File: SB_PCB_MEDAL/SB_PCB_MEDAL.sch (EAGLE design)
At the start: 10 parts, among them IC1 ATTINY44A-SSU

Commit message: completed circuit for charliplexed LEDs
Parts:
- added LED10, LED11, LED12, LED13, LED14, LED15, LED16, LED18, LED19, LED2, LED20, LED21, LED22, LED23, LED24, LED25, LED26, LED27, LED28, LED29, LED3, LED30, LED31, LED32, LED33, LED4, LED5, LED6, LED7, LED8, LED9: KPT-2012CGCK, SamacSys_Parts:KPT-2012CGCK
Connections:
- new net N$1: LED26.A
- new net N$10: LED2.A, LED4.K
- new net N$2: LED3.K, LED5.A, LED7.A
- new net N$3: LED1.K, LED3.A
- new net N$4: LED5.K, LED7.K, LED8.A, LED9.A
- new net N$5: LED11.A, LED8.K, LED9.K
- new net N$6: LED10.A, LED12.K
- new net N$7: LED10.K, LED6.A
- new net N$8: LED4.A, LED6.K
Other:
- moved on the sheet: R2, R3, R4, R5, R6

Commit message: re-did some wiring
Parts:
- removed LED31, LED32, LED33: KPT-2012CGCK, SamacSys_Parts:KPT-2012CGCK
- added LED17: KPT-2012CGCK, SamacSys_Parts:KPT-2012CGCK
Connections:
- removed net N$10: LED2.A, LED4.K
- removed net N$7: LED10.K, LED6.A
- removed net N$8: LED4.A, LED6.K
- net N$1: now also LED1.A, LED11.A, LED12.K, LED19.A, LED2.K, LED20.K, LED25.A, LED26.K, LED29.A, LED30.K, R1.2; no longer LED26.A
- net N$2: now also LED1.K, LED13.A, LED14.K, LED2.A, LED21.A, LED22.K, LED27.A, LED28.K, LED3.A, LED4.K, R2.2; no longer LED3.K, LED5.A, LED7.A
- net N$3: now also LED11.K, LED12.A, LED15.A, LED16.K, LED23.A, LED24.K, LED3.K, LED4.A, LED5.A, LED6.K, R3.2; no longer LED1.K, LED3.A
- net N$4: now also LED13.K, LED14.A, LED17.A, LED18.K, LED19.K, LED20.A, LED6.A, LED7.A, LED8.K, R4.2; no longer LED7.K, LED8.A, LED9.A
- net N$5: now also LED10.K, LED15.K, LED16.A, LED21.K, LED22.A, LED25.K, LED26.A, LED7.K, LED8.A, LED9.A, R5.2; no longer LED11.A, LED8.K, LED9.K
- net N$6: now also LED17.K, LED18.A, LED23.K, LED24.A, LED27.K, LED28.A, LED29.K, LED30.A, LED9.K, R6.2; no longer LED12.K
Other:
- moved on the sheet: LED1, LED10, LED11, LED12, LED13, LED14, LED15, LED16, LED18, LED19, LED2, LED20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

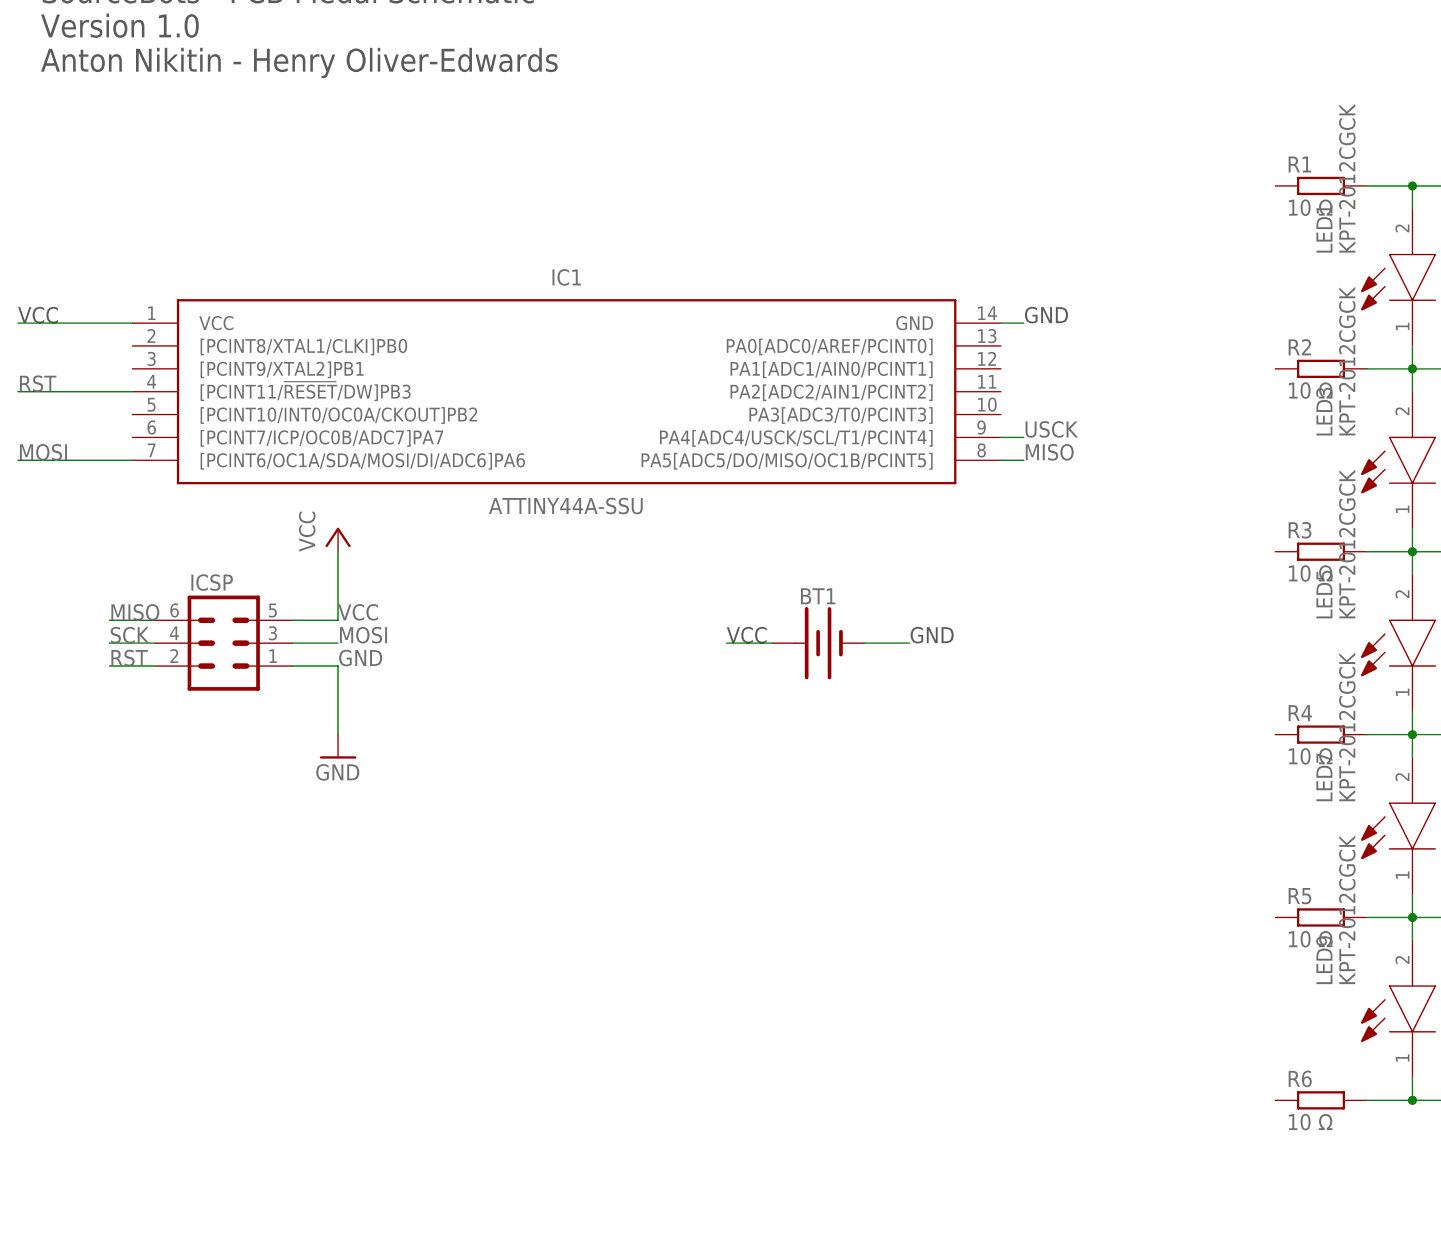
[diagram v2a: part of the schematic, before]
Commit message: added labels to pins
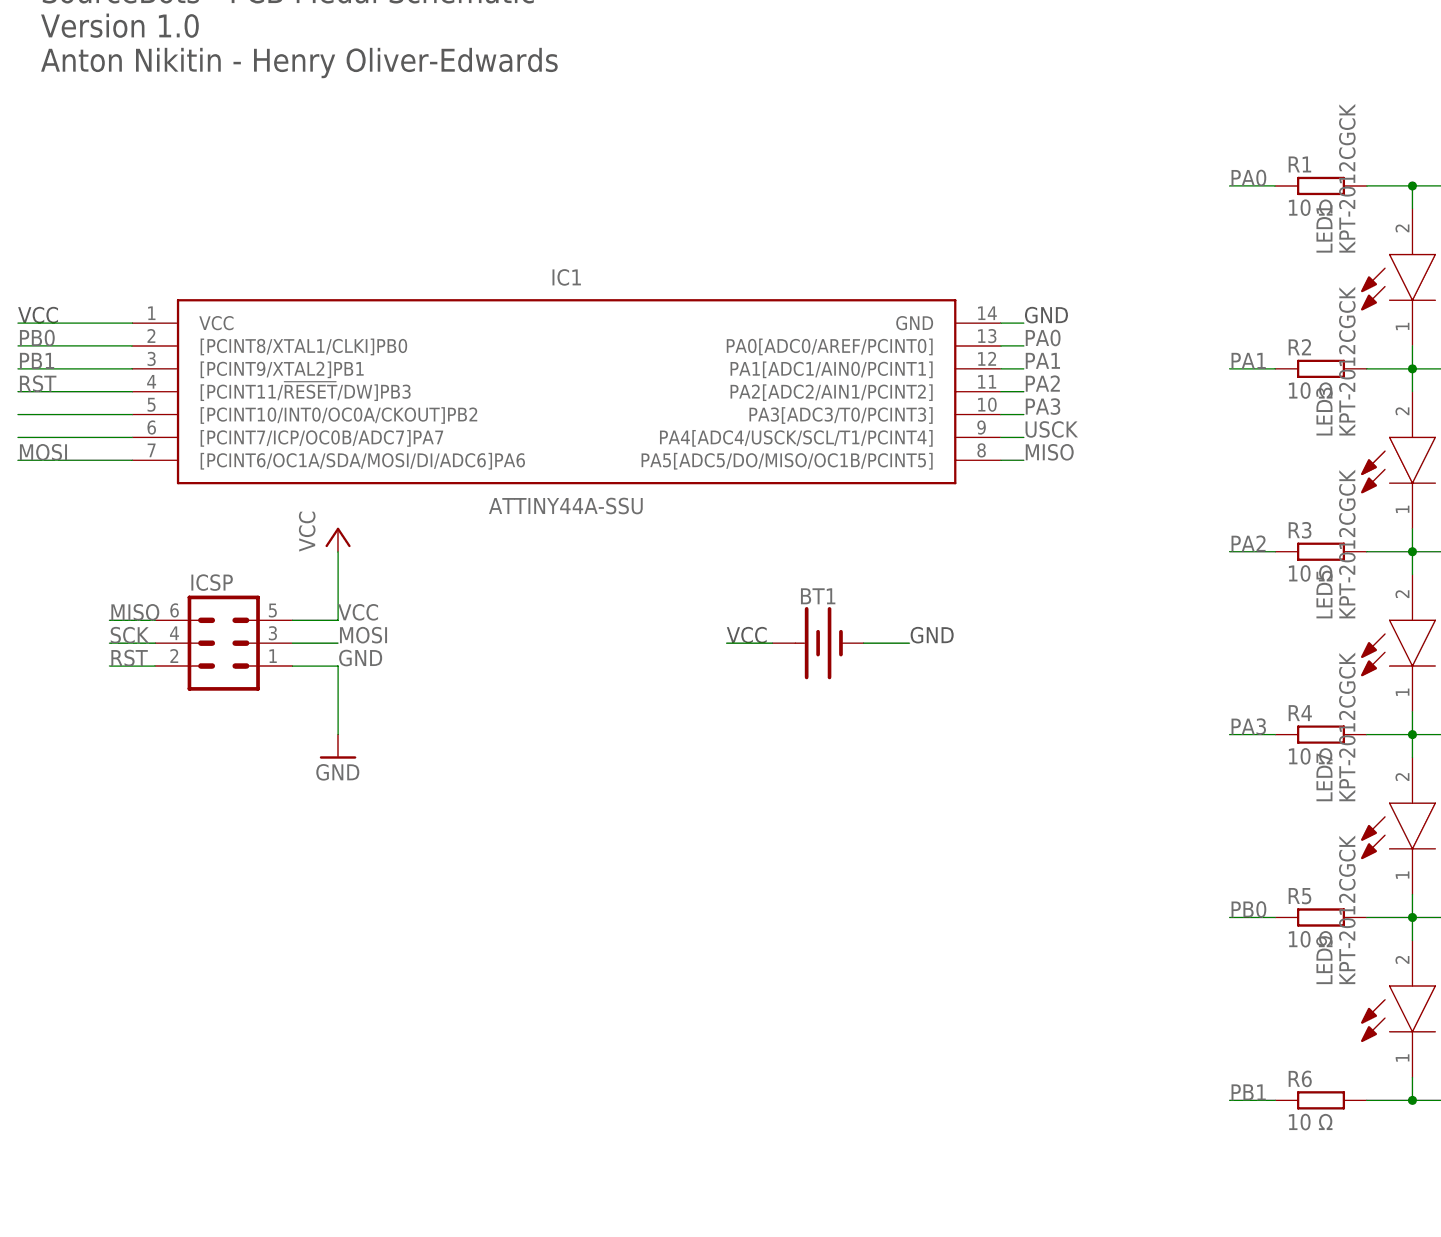
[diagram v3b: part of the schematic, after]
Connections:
- new net N$19: IC1.[PCINT10/INT0/OC0A/CKOUT]PB2
- new net N$20: IC1.[PCINT7/ICP/OC0B/ADC7]PA7
- new net PA0: IC1.PA0[ADC0/AREF/PCINT0], R1.1
- new net PA1: IC1.PA1[ADC1/AIN0/PCINT1], R2.1
- new net PA2: IC1.PA2[ADC2/AIN1/PCINT2], R3.1
- new net PA3: IC1.PA3[ADC3/T0/PCINT3], R4.1
- new net PB0: IC1.[PCINT8/XTAL1/CLKI]PB0, R5.1
- new net PB1: IC1.[PCINT9/XTAL2]PB1, R6.1
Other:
- note added: "PA0"
- note added: "PA1"
- note added: "PA2"
- note added: "PA3"
- note added: "PB0"
- note added: "PB1"
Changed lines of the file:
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@@
 <?xml version="1.0" encoding="utf-8"?>
 <!DOCTYPE eagle SYSTEM "eagle.dtd">
-<eagle version="8.3.1">
+<eagle version="8.4.3">
 <drawing>
 <settings>
@@
 <text x="78.74" y="30.48" size="1.778" layer="97">GND</text>
 <text x="58.42" y="30.48" size="1.778" layer="97">VCC</text>
+<text x="91.44" y="63.5" size="1.778" layer="95">PA0</text>
+<text x="91.44" y="60.96" size="1.778" layer="95">PA1</text>
+<text x="91.44" y="58.42" size="1.778" layer="95">PA2</text>
+<text x="91.44" y="55.88" size="1.778" layer="95">PA3</text>
+<text x="-20.32" y="63.5" size="1.778" layer="95">PB0</text>
+<text x="-20.32" y="60.96" size="1.778" layer="95">PB1</text>
+<text x="114.3" y="81.28" size="1.778" layer="95">PA0</text>
+<text x="114.3" y="60.96" size="1.778" layer="95">PA1</text>
+<text x="114.3" y="40.64" size="1.778" layer="95">PA2</text>
+<text x="114.3" y="20.32" size="1.778" layer="95">PA3</text>
+<text x="114.3" y="0" size="1.778" layer="95">PB0</text>
+<text x="114.3" y="-20.32" size="1.778" layer="95">PB1</text>
 </plain>
 <instances>
@@
 </segment>
 </net>
+<net name="PA0" class="0">
+<segment>
+<pinref part="IC1" gate="G$1" pin="PA0[ADC0/AREF/PCINT0]"/>
+<wire x1="88.9" y1="63.5" x2="91.44" y2="63.5" width="0.1524" layer="91"/>
+</segment>
+<segment>
+<pinref part="R1" gate="G$1" pin="1"/>
+<wire x1="119.38" y1="81.28" x2="114.3" y2="81.28" width="0.1524" layer="91"/>
+</segment>
+</net>
+<net name="PA1" class="0">
+<segment>
+<pinref part="IC1" gate="G$1" pin="PA1[ADC1/AIN0/PCINT1]"/>
+<wire x1="88.9" y1="60.96" x2="91.44" y2="60.96" width="0.1524" layer="91"/>
+</segment>
+<segment>
+<pinref part="R2" gate="G$1" pin="1"/>
+<wire x1="119.38" y1="60.96" x2="114.3" y2="60.96" width="0.1524" layer="91"/>
+</segment>
+</net>
+<net name="PA2" class="0">
+<segment>
+<pinref part="IC1" gate="G$1" pin="PA2[ADC2/AIN1/PCINT2]"/>
+<wire x1="88.9" y1="58.42" x2="91.44" y2="58.42" width="0.1524" layer="91"/>
+</segment>
+<segment>
+<pinref part="R3" gate="G$1" pin="1"/>
+<wire x1="119.38" y1="40.64" x2="114.3" y2="40.64" width="0.1524" layer="91"/>
+</segment>
+</net>
+<net name="PA3" class="0">
+<segment>
+<pinref part="IC1" gate="G$1" pin="PA3[ADC3/T0/PCINT3]"/>
+<wire x1="88.9" y1="55.88" x2="91.44" y2="55.88" width="0.1524" layer="91"/>
+</segment>
+<segment>
+<pinref part="R4" gate="G$1" pin="1"/>
+<wire x1="119.38" y1="20.32" x2="114.3" y2="20.32" width="0.1524" layer="91"/>
+</segment>
+</net>
+<net name="PB0" class="0">
+<segment>
+<pinref part="IC1" gate="G$1" pin="[PCINT8/XTAL1/CLKI]PB0"/>
+<wire x1="-7.62" y1="63.5" x2="-20.32" y2="63.5" width="0.1524" layer="91"/>
+</segment>
+<segment>
+<pinref part="R5" gate="G$1" pin="1"/>
+<wire x1="119.38" y1="0" x2="114.3" y2="0" width="0.1524" layer="91"/>
+</segment>
+</net>
+<net name="PB1" class="0">
+<segment>
+<pinref part="IC1" gate="G$1" pin="[PCINT9/XTAL2]PB1"/>
+<wire x1="-7.62" y1="60.96" x2="-20.32" y2="60.96" width="0.1524" layer="91"/>
+</segment>
+<segment>
+<pinref part="R6" gate="G$1" pin="1"/>
+<wire x1="119.38" y1="-20.32" x2="114.3" y2="-20.32" width="0.1524" layer="91"/>
+</segment>
+</net>
+<net name="N$19" class="0">
+<segment>
+<pinref part="IC1" gate="G$1" pin="[PCINT10/INT0/OC0A/CKOUT]PB2"/>
+<wire x1="-7.62" y1="55.88" x2="-20.32" y2="55.88" width="0.1524" layer="91"/>
+</segment>
+</net>
+<net name="N$20" class="0">
+<segment>
+<pinref part="IC1" gate="G$1" pin="[PCINT7/ICP/OC0B/ADC7]PA7"/>
+<wire x1="-7.62" y1="53.34" x2="-20.32" y2="53.34" width="0.1524" layer="91"/>
+</segment>
+</net>

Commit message: modify board
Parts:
- removed IC1: ATTINY44A-SSU, SamacSys_Parts:ATTINY44A-SSU
- added U1: ATMEGA16U2-AU, Atmel_By_element14_Batch_1-00:ATMEGA16U2-AU
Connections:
- removed net N$19: IC1.[PCINT10/INT0/OC0A/CKOUT]PB2
- removed net N$20: IC1.[PCINT7/ICP/OC0B/ADC7]PA7
- net GND: no longer IC1.GND
- net MISO: no longer IC1.PA5[ADC5/DO/MISO/OC1B/PCINT5]
- net MOSI: no longer IC1.[PCINT6/OC1A/SDA/MOSI/DI/ADC6]PA6
- net PA0: no longer IC1.PA0[ADC0/AREF/PCINT0]
- net PA1: no longer IC1.PA1[ADC1/AIN0/PCINT1]
- net PA2: no longer IC1.PA2[ADC2/AIN1/PCINT2]
- net PA3: no longer IC1.PA3[ADC3/T0/PCINT3]
- net PB0: no longer IC1.[PCINT8/XTAL1/CLKI]PB0
- net PB1: no longer IC1.[PCINT9/XTAL2]PB1
- net RST: no longer IC1.[PCINT11/!RESET!/DW]PB3
- net USCK: no longer IC1.PA4[ADC4/USCK/SCL/T1/PCINT4]
- net VCC: no longer IC1.VCC
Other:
- note added: "1"
- note added: "ATMEGA16U2-AU Microcontroller"
- note added: "Anton Nikitin - Henry Oliver-Edwards"
- note added: "Battery"
- note added: "CC 2.5 BY/SA"
- note added: "Charlieplexing Circuit for LEDs"
- note added: "ICSP Header"
- note added: "SourceBots - PCB Medals"
- note added: "v1.0"
- note removed: "SourceBots - PCB Medal Schematic Version 1.0 Anton Nikitin - Henry Oliver-Edwards"
- note removed: "USCK"
- moved on the sheet: BT1, ICSP, LED1, LED10, LED11, LED12, LED13, LED14, LED15, LED16, LED17, LED18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
